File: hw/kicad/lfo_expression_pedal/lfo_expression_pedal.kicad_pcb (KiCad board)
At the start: 2 copper layers, 53.3 x 61 mm, 34 parts, among them J1 Conn_02x05_Odd_Even, J2 Conn_01x03, J4 Conn_01x02, J5 Conn_01x04, J6 Conn_01x03, SW1 SW_SPST, SW2 SW_SPST, SW3 SW_SPST, SW4 SW_SPST, SW5 SW_SPST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

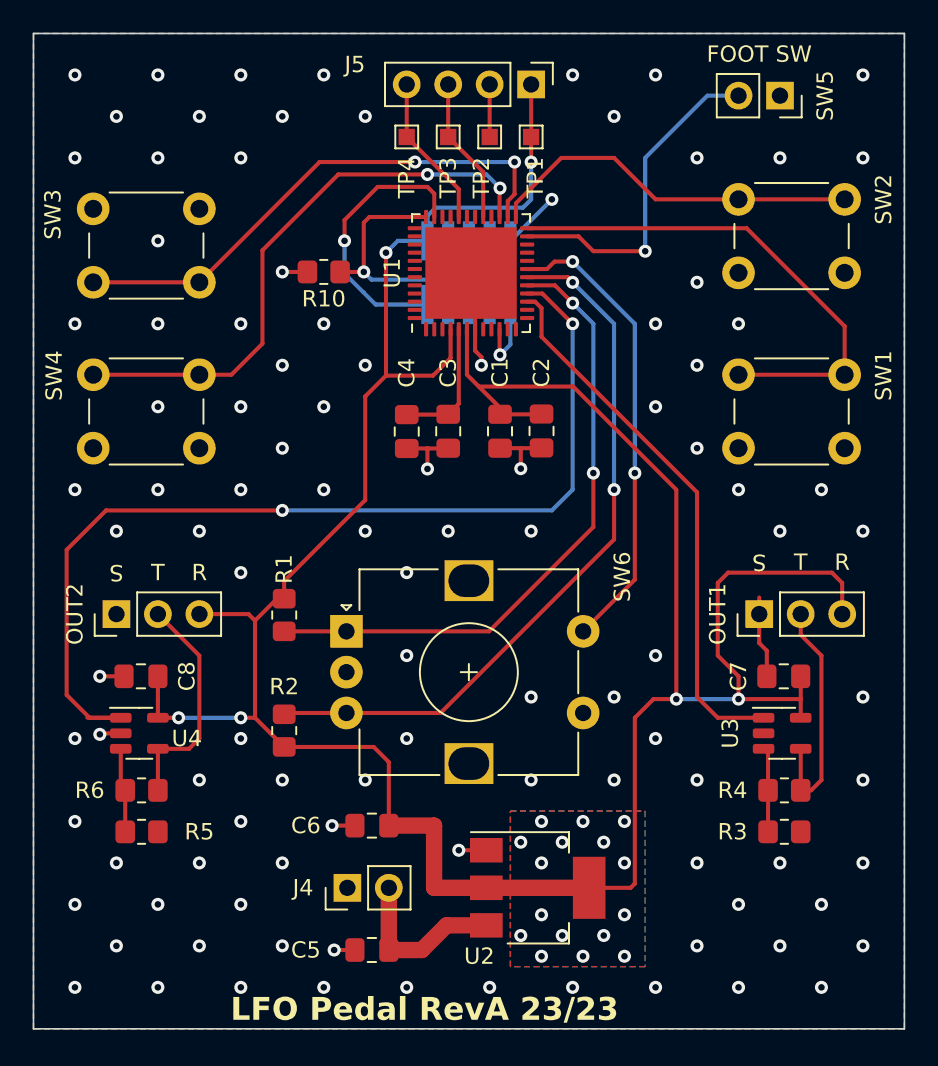
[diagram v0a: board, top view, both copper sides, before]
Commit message: Add 3.3v to U1 VREF+ (Pin5)
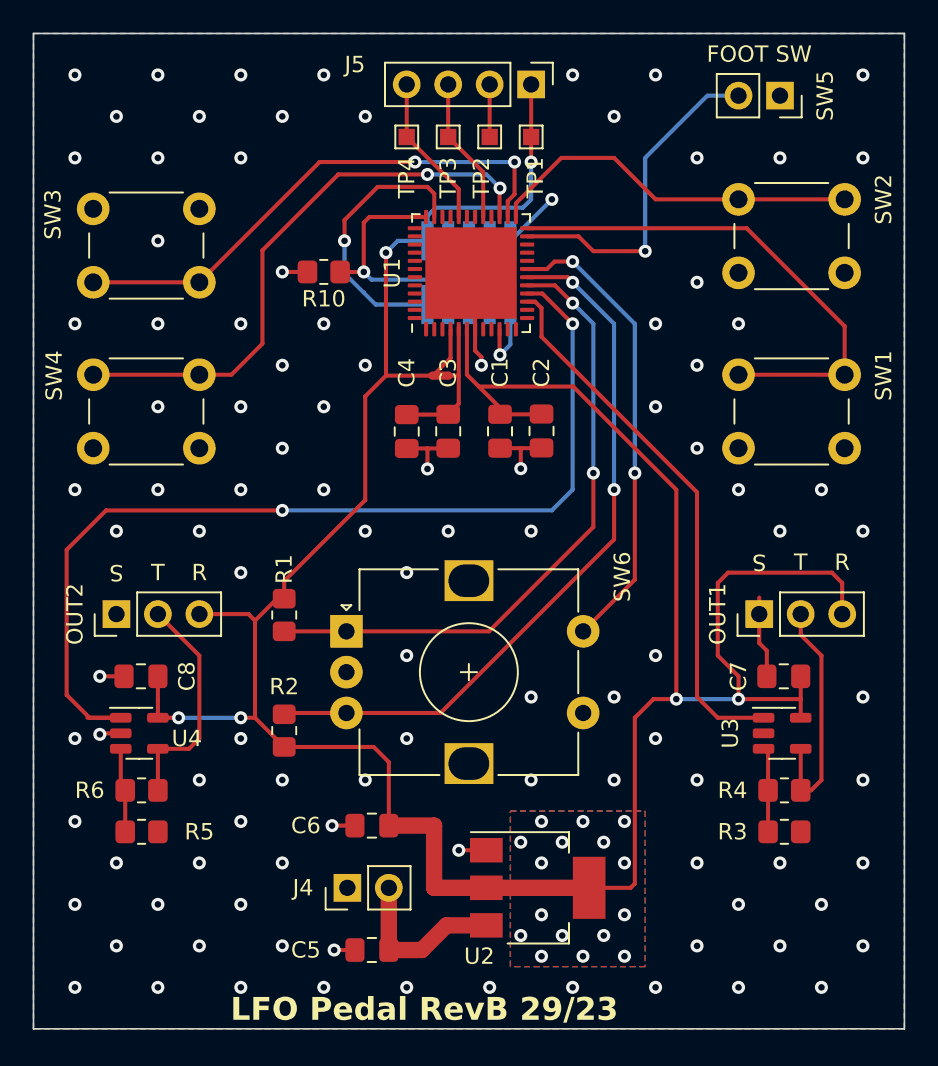
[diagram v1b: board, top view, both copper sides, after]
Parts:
- added NT1: NetTie_2, NetTie:NetTie-2_SMD_Pad0.5mm, F.Cu at (139.2, 84.5)
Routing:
- net /vref: track 8.47 -> 9.09 mm
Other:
- board text added: "LFO Pedal RevB 29/23"
- board text removed: "LFO Pedal RevA 23/23"
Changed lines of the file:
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@@
     (descr "Resistor SMD 0805 (2012 Metric), square (rectangular) end terminal, IPC_7351 nominal with elongated pad for handsoldering. (Body size source: IPC-SM-782 page 72, https://www.pcb-3d.com/wordpress/wp-content/uploads/ipc-sm-782a_amendment_1_and_2.pdf), generated with kicad-footprint-generator")
     (tags "resistor handsolder")
-    (property "LCSC MPN" "C5140080")
+    (property "LCSC MPN" "C103914")
     (property "Sheetfile" "lfo_expression_pedal.kicad_sch")
     (property "Sheetname" "")
@@
     )
   )
+  (footprint "NetTie:NetTie-2_SMD_Pad0.5mm" (layer "F.Cu")
+    (at 139.2254 84.455 180)
+    (descr "Net tie, 2 pin, 0.5mm square SMD pads")
+    (tags "net tie")
+    (property "Sheetfile" "lfo_expression_pedal.kicad_sch")
+    (property "Sheetname" "")
+    (property "exclude_from_bom" "")
+    (property "ki_description" "Net tie, 2 pins")
+    (property "ki_keywords" "net tie short")
+    (attr exclude_from_pos_files exclude_from_bom)
+    (net_tie_pad_groups "1, 2")
+    (fp_text reference "NT1" (at 0 -1.2) (layer "F.SilkS") hide
+        (effects (font (size 1 1) (thickness 0.15)))
+    )
+    (fp_text value "NetTie_2" (at 0 1.2) (layer "F.Fab")
+        (effects (font (size 1 1) (thickness 0.15)))
+    )
+    (fp_poly
+      (pts
+        (xy -0.5 -0.25)
+        (xy 0.5 -0.25)
+        (xy 0.5 0.25)
+        (xy -0.5 0.25)
+      )
+      (stroke (width 0) (type solid)) (fill solid) (layer "F.Cu"))
+    (fp_line (start -1 -0.5) (end -1 0.5)
+      (stroke (width 0.05) (type solid)) (layer "F.CrtYd"))
+    (fp_line (start -1 0.5) (end 1 0.5)
+      (stroke (width 0.05) (type solid)) (layer "F.CrtYd"))
+    (fp_line (start 1 -0.5) (end -1 -0.5)
+      (stroke (width 0.05) (type solid)) (layer "F.CrtYd"))
+    (fp_line (start 1 0.5) (end 1 -0.5)
+      (stroke (width 0.05) (type solid)) (layer "F.CrtYd"))
+    (pad "1" smd circle (at -0.5 0 180) (size 0.5 0.5) (layers "F.Cu")
+      (net 9 "/vref") (pinfunction "1") (pintype "passive"))
+    (pad "2" smd circle (at 0.5 0 180) (size 0.5 0.5) (layers "F.Cu")
+      (net 1 "+3.3V") (pinfunction "2") (pintype "passive"))
+  )
   (footprint "Capacitor_SMD:C_0805_2012Metric_Pad1.18x1.45mm_HandSolder" (layer "F.Cu")
     (at 120.8825 102.87 180)
@@
     (descr "Resistor SMD 0805 (2012 Metric), square (rectangular) end terminal, IPC_7351 nominal with elongated pad for handsoldering. (Body size source: IPC-SM-782 page 72, https://www.pcb-3d.com/wordpress/wp-content/uploads/ipc-sm-782a_amendment_1_and_2.pdf), generated with kicad-footprint-generator")
     (tags "resistor handsolder")
-    (property "LCSC MPN" "C5140080")
+    (property "LCSC MPN" "C2907288")
     (property "Sheetfile" "lfo_expression_pedal.kicad_sch")
     (property "Sheetname" "")
@@
     (descr "Resistor SMD 0805 (2012 Metric), square (rectangular) end terminal, IPC_7351 nominal with elongated pad for handsoldering. (Body size source: IPC-SM-782 page 72, https://www.pcb-3d.com/wordpress/wp-content/uploads/ipc-sm-782a_amendment_1_and_2.pdf), generated with kicad-footprint-generator")
     (tags "resistor handsolder")
-    (property "LCSC MPN" "C5140080")
+    (property "LCSC MPN" "C2907288")
     (property "Sheetfile" "lfo_expression_pedal.kicad_sch")
     (property "Sheetname" "")
@@
   (gr_line (start 114.3 63.5) (end 167.64 63.5)
     (stroke (width 0.1) (type default)) (layer "Edge.Cuts"))
-  (gr_text "LFO Pedal RevA 23/23" (at 126.365 124.079) (layer "F.SilkS")
+  (gr_text "LFO Pedal RevB 29/23" (at 126.365 124.079) (layer "F.SilkS")
     (effects (font (size 1.4 1.4) (thickness 0.3) bold) (justify left bottom))
   )
@@
   (segment (start 140.347 74.7395) (end 140.347 73.0249) (width 0.25) (layer "F.Cu") (net 8))
   (segment (start 137.16 69.8379) (end 137.16 66.62) (width 0.25) (layer "F.Cu") (net 8))
+  (segment (start 140.347 84.455) (end 140.347 86.178) (width 0.25) (layer "F.Cu") (net 9))
+  (segment (start 139.7254 84.455) (end 140.347 84.455) (width 0.25) (layer "F.Cu") (net 9))
+  (segment (start 140.347 81.4995) (end 140.347 84.455) (width 0.25) (layer "F.Cu") (net 9))
   (segment (start 139.6825 86.8425) (end 136.8325 86.8425) (width 0.25) (layer "F.Cu") (net 9))
-  (segment (start 140.347 81.4995) (end 140.347 86.178) (width 0.25) (layer "F.Cu") (net 9))
   (segment (start 140.347 86.178) (end 139.6825 86.8425) (width 0.25) (layer "F.Cu") (net 9))
   (segment (start 147.32 80.01) (end 146.237 78.927) (width 0.25) (layer "F.Cu") (net 10))
